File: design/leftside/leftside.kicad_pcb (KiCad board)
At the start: 4 copper layers, 142.6 x 96.2 mm, 211 parts, among them IC2 XC9148G50CER-G, IC3 nRF52833-QDAA-R7, IC4 74AHCT125PW,118, IC5 MCP23018T-E_SS, IC6 XC9291B33D1R-G, J1 USB_C_Receptacle_USB2.0_16P, J2 Battery Pos, J3 Battery Neg, J4 OLED_128x32, J6 Conn_01x04, J7 F32Q-1A7H1-11012, U1 BQ27441-G1, U2 BQ24072RGT, U3 USB6B1, U5 PEC11L-4015F-S0015, U6 PEC11L-4015F-S0015, Y1 ECS-320-8-37B2-JTY-TR

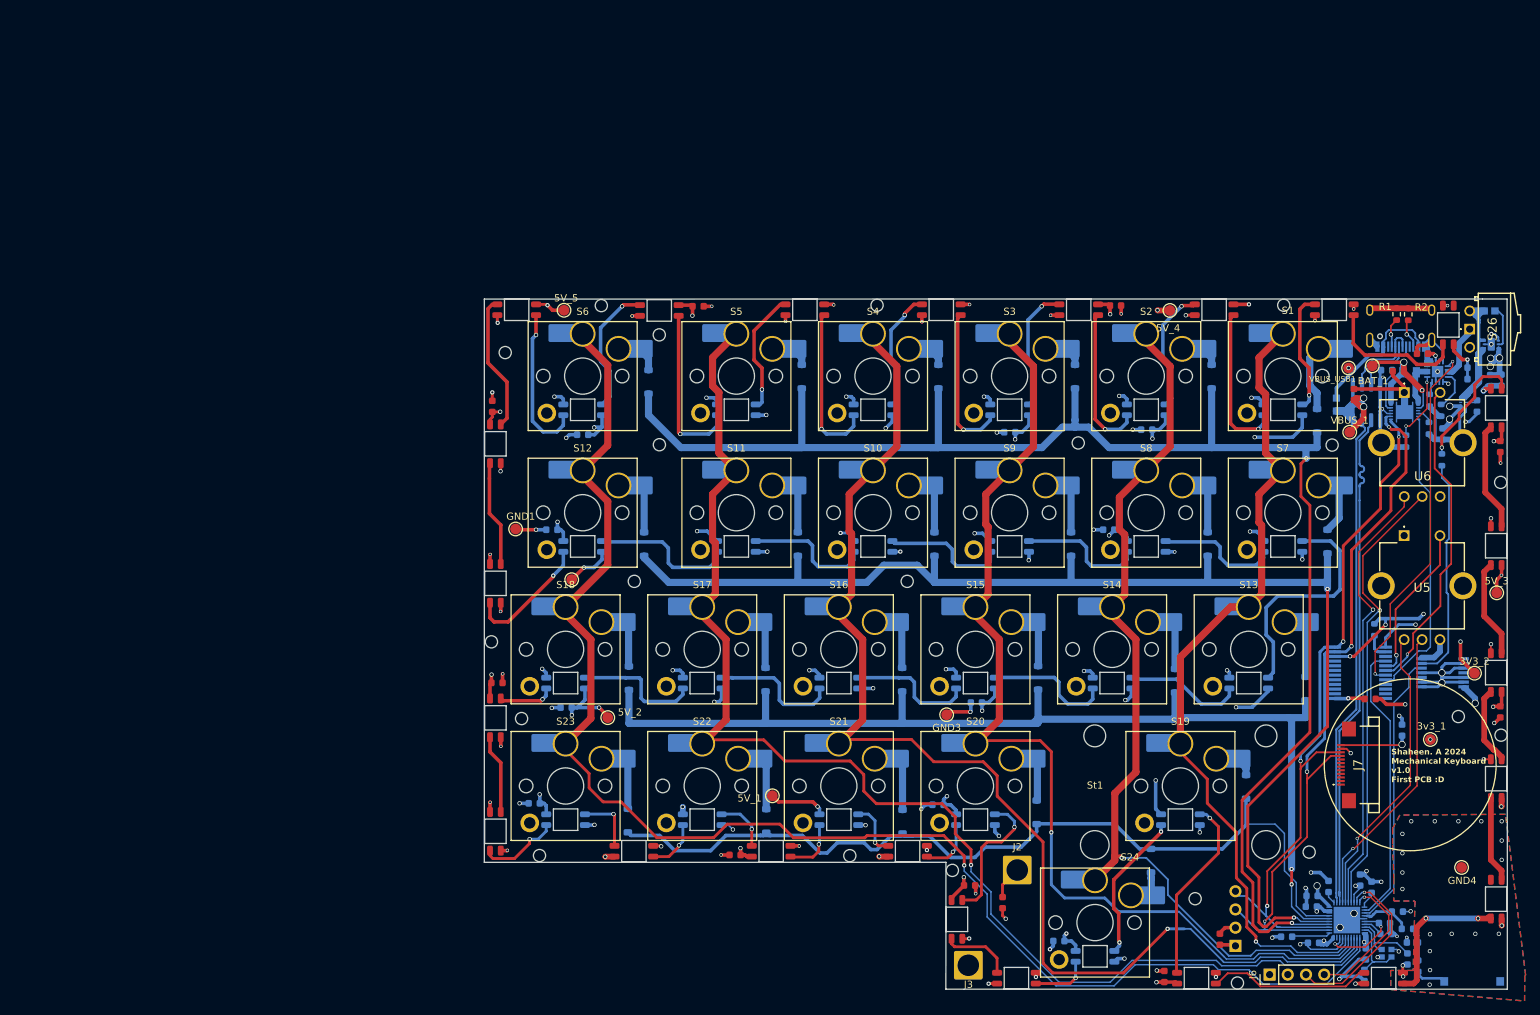
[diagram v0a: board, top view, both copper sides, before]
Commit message: expand power planes
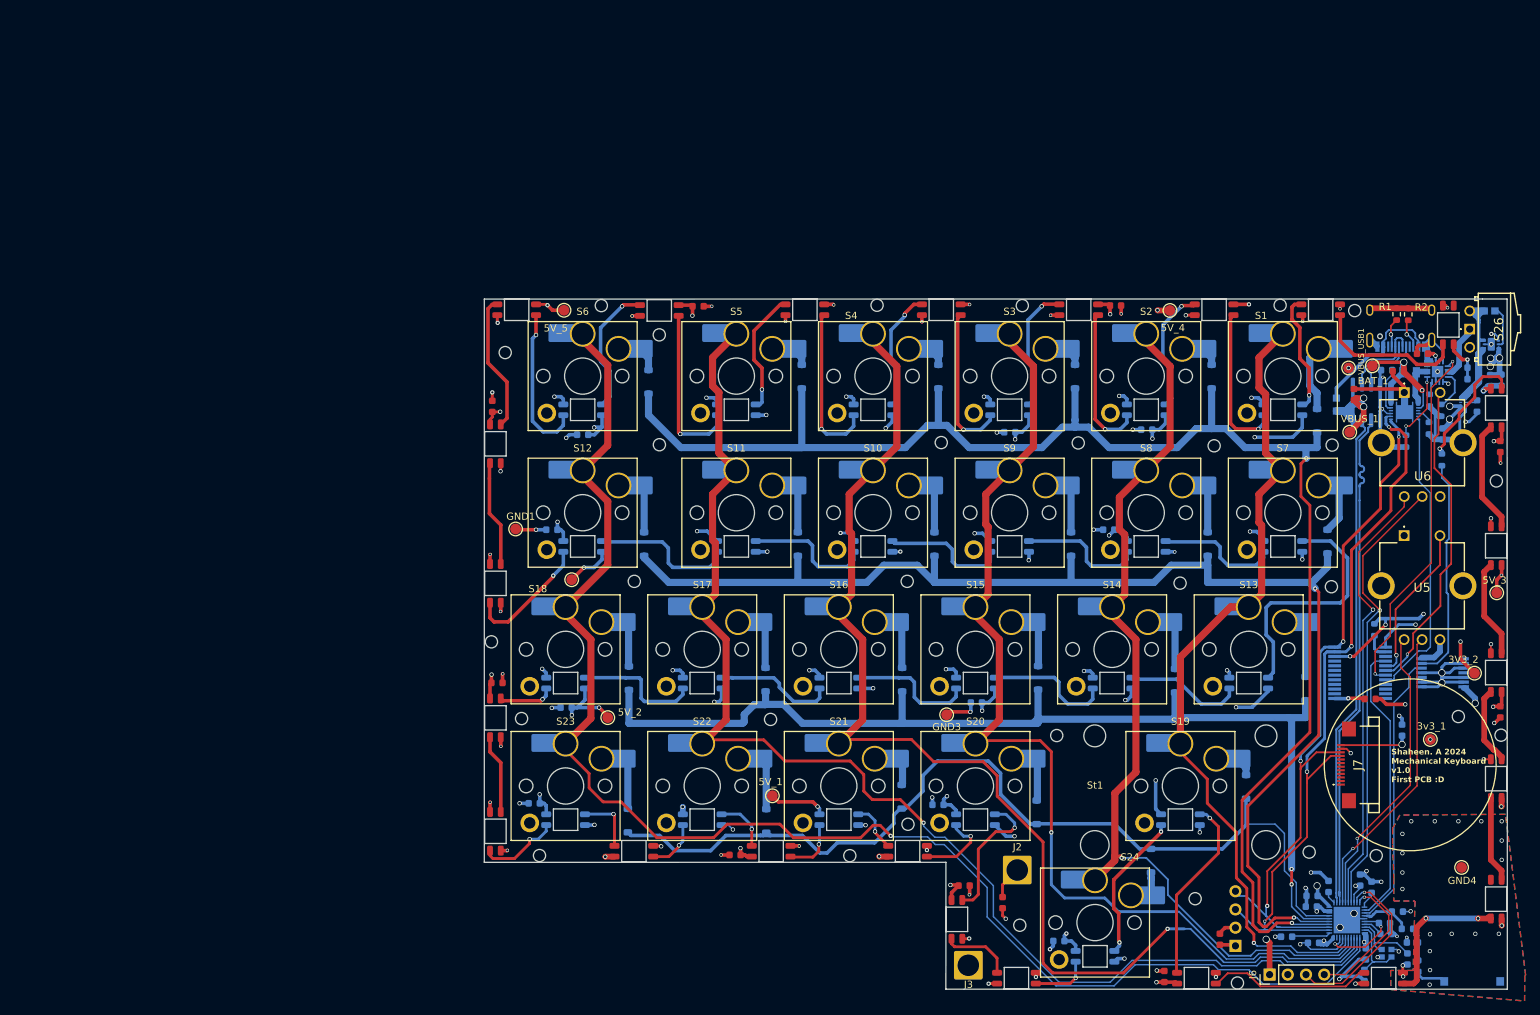
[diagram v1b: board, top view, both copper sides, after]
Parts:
- added REF**: M1.6 Hole, CustomLibrary:M1.6 Hole, F.Cu at (147.2, 75.0)
- added REF**: M1.6 Hole, CustomLibrary:M1.6 Hole, F.Cu at (158.2, 142.3)
- added REF**: M1.6 Hole, CustomLibrary:M1.6 Hole, F.Cu at (163.3, 115.9)
- added REF**: M1.6 Hole, CustomLibrary:M1.6 Hole, F.Cu at (180.5, 94.6)
- added REF**: M1.6 Hole, CustomLibrary:M1.6 Hole, F.Cu at (185.3, 75.5)
- added REF**: M1.6 Hole, CustomLibrary:M1.6 Hole, F.Cu at (207.9, 132.6)
- added REF**: M1.6 Hole, CustomLibrary:M1.6 Hole, F.Cu at (123.4, 113.6)
- added REF**: M1.6 Hole, CustomLibrary:M1.6 Hole, F.Cu at (204.9, 56.6)
- added REF**: M1.6 Hole, CustomLibrary:M1.6 Hole, F.Cu at (158.5, 55.9)
- added REF**: M1.6 Hole, CustomLibrary:M1.6 Hole, F.Cu at (201.6, 95.1)
- moved REF** 8.93 mm to (142.6, 128.3)
- moved Di6 3.47 mm to (141.7, 124.4)
- moved D47 1.90 mm to (200.1, 56.5)
- moved C31 0.76 mm to (150.4, 136.8)
- moved REF** 0.63 mm to (224.6, 80.4)
- moved REF** 0.50 mm to (194.5, 55.9)
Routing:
- net 3V3: track 63.9 -> 69.1 mm, vias 14 -> 15
- net /Row 3: track 127.7 -> 132.1 mm
- net Net-(Di6-A): track 7.55 -> 4.13 mm
- net Net-(D12-DOUT): track 8.02 -> 10.8 mm
- net /Column 4: track 181.5 -> 179.3 mm
- net /Row 0: track 218.9 -> 216.8 mm
- net Net-(D26-DOUT): track 33.1 -> 35.1 mm
- net Net-(D47-DOUT): track 19.9 -> 21.5 mm
- net /Row 1: track 181.8 -> 183.3 mm
- net Net-(D22-DOUT): track 18.3 -> 16.9 mm
- net Net-(D13-DOUT): track 7.82 -> 7.01 mm
- net GND: track 270.3 -> 271.0 mm

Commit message: RS LS Complete
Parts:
- moved R6 0.68 mm to (212.5, 65.9)
- moved C23 0.63 mm to (214.3, 63.3)
- moved BAT_1 0.58 mm to (207.5, 64.9)
- moved C18 0.50 mm to (211.1, 65.6)
- moved D10 0.33 mm to (157.4, 149.7)
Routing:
- net Net-(D47-DOUT): track 21.5 -> 22.9 mm
- net GND: track 271.0 -> 271.7 mm
- net 5V: track 168.0 -> 167.4 mm

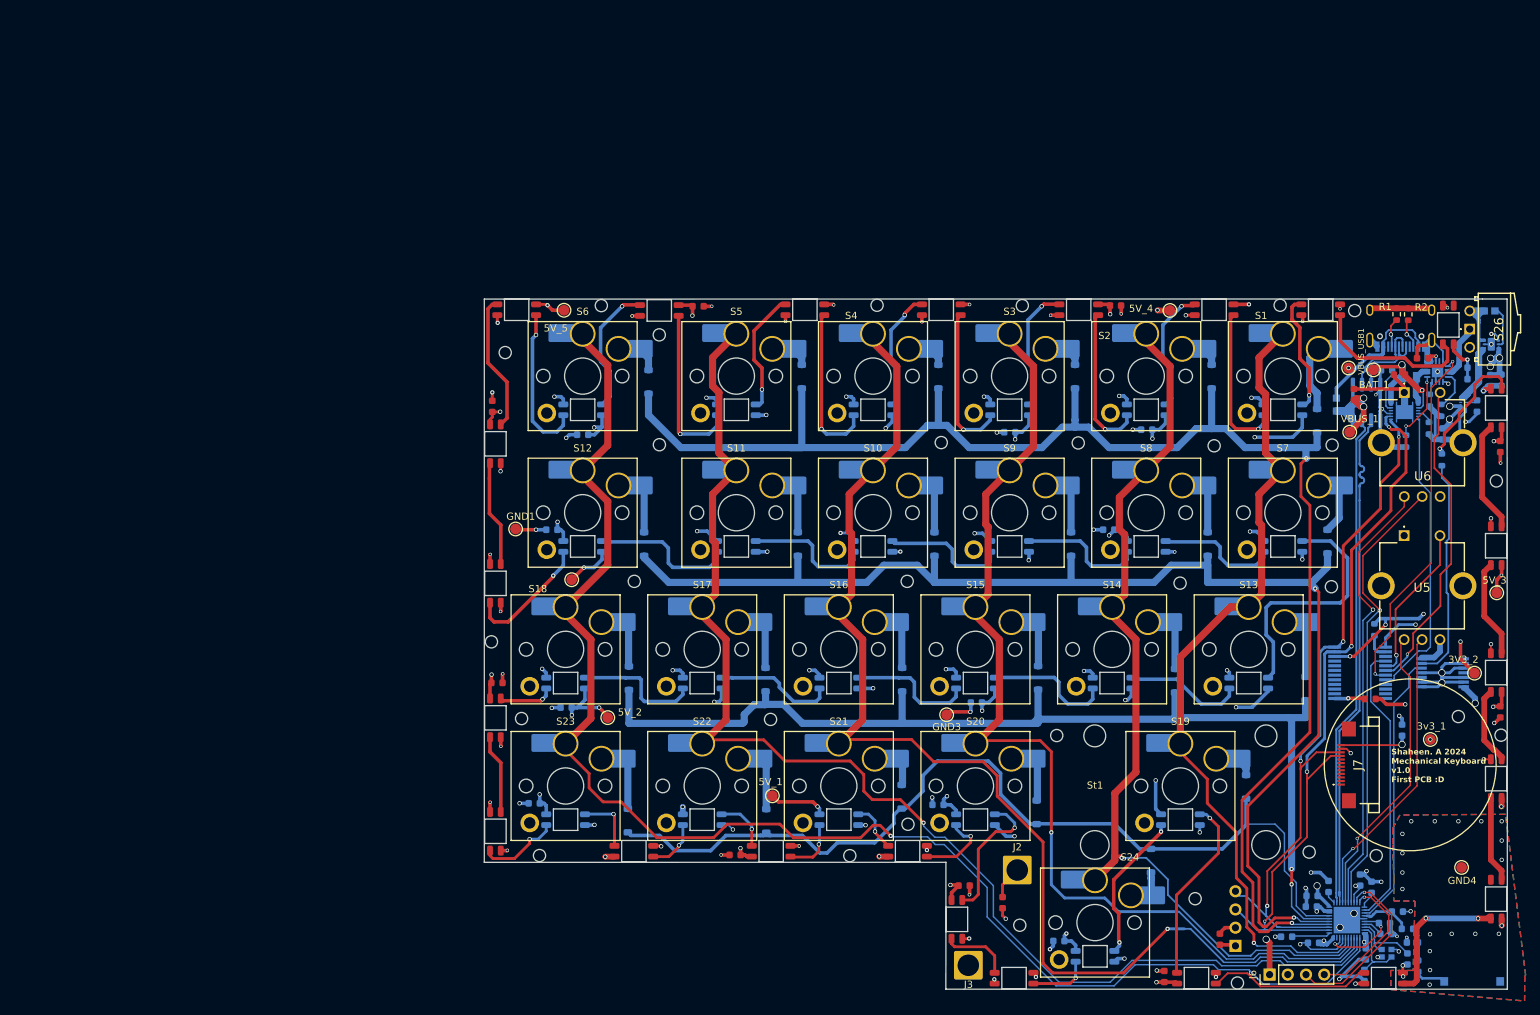
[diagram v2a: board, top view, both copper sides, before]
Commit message: create first merged gerber, prepare to fix board outline
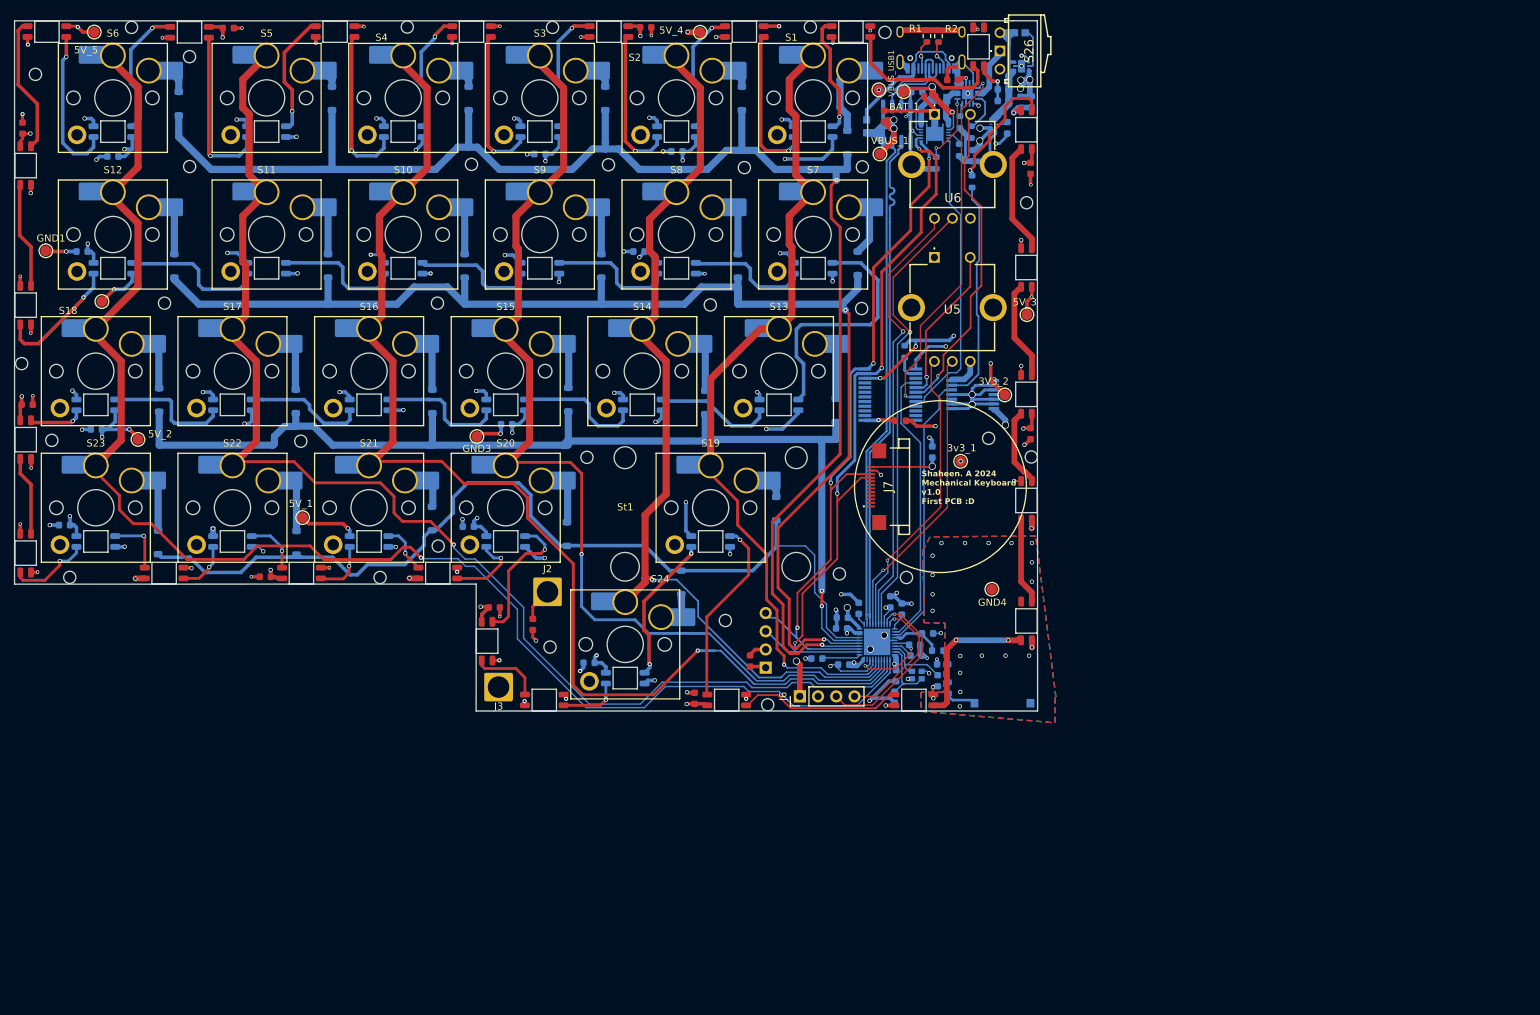
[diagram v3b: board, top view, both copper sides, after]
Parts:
- moved REF** 76.1 mm to (117.1, 99.9)
- moved 3V3_2 76.1 mm to (156.1, 68.4)
- moved 3v3_1 76.1 mm to (149.9, 77.7)
- moved 5V_1 76.1 mm to (58.2, 85.5)
- moved 5V_2 76.1 mm to (35.2, 74.6)
- moved 5V_4 76.1 mm to (113.6, 17.8)
- moved 5V_5 76.1 mm to (29.1, 17.8)
- moved ANT1 76.1 mm to (155.7, 111.4)
- moved BAT_1 76.1 mm to (142.0, 26.1)
- moved C1 76.1 mm to (133.3, 101.0)
- moved C10 76.1 mm to (155.9, 25.8)
- moved C13 76.1 mm to (151.6, 35.1)
- moved C14 76.1 mm to (140.7, 110.6)
- moved C15 76.1 mm to (147.4, 106.0)
- moved C16 76.1 mm to (145.3, 101.7)
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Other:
- outline, holes or cut-outs redrawn

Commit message: submit merged design and do proper outline for boards
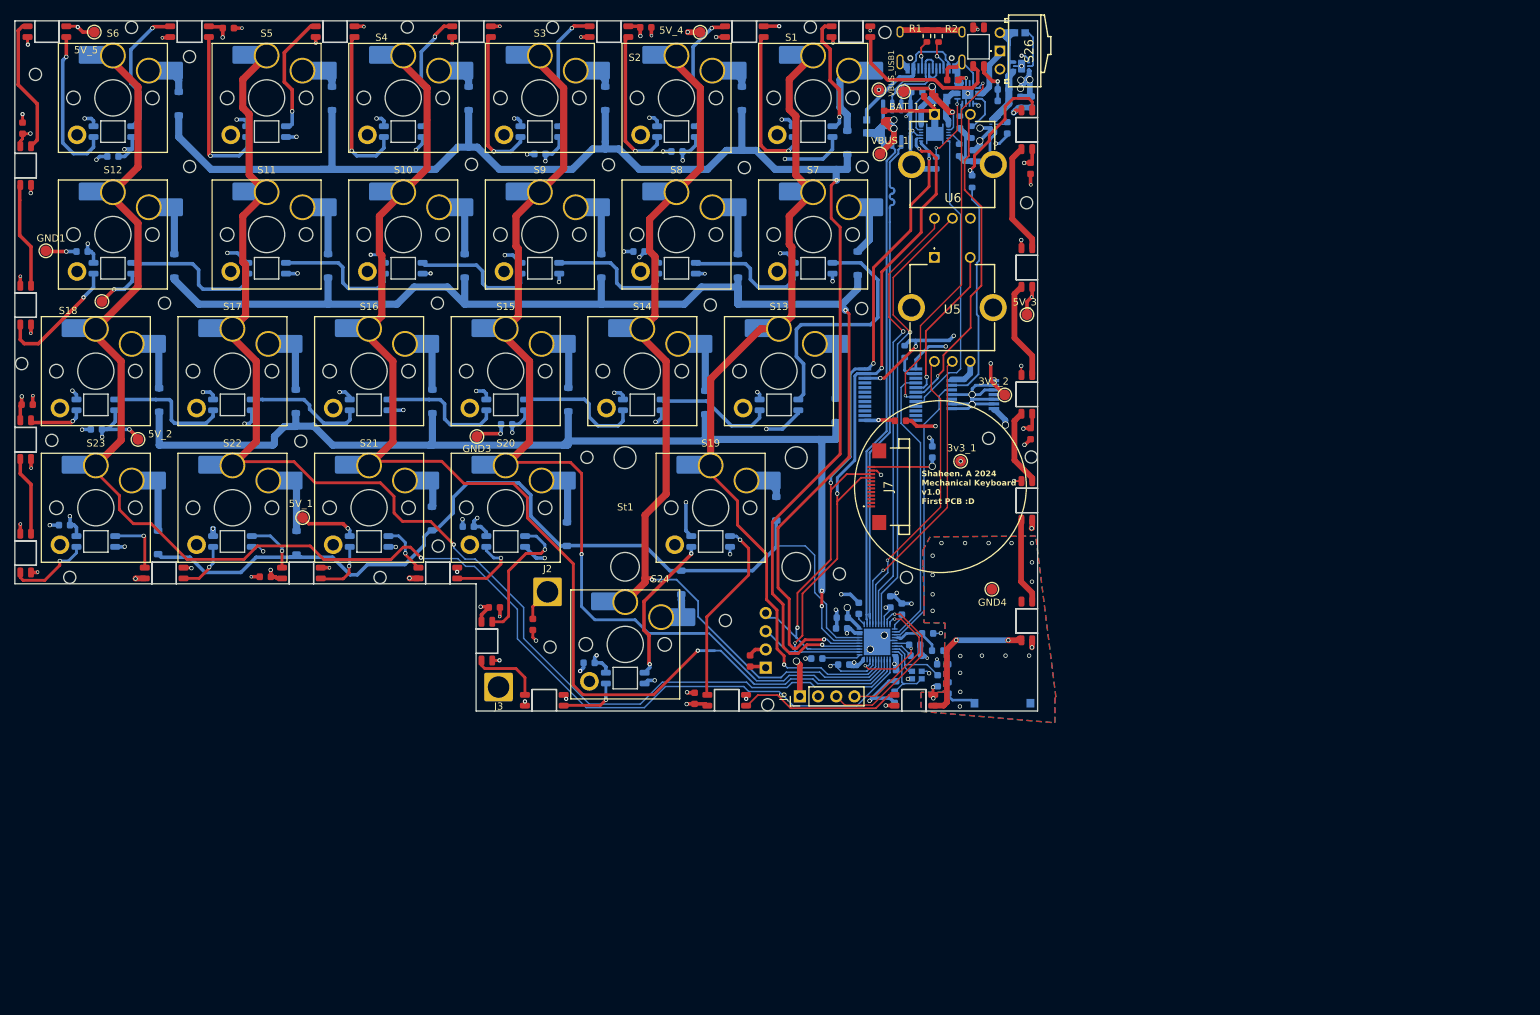
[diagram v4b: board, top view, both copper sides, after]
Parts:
- moved D37 0.09 mm to (42.4, 17.7)
- moved D1 0.05 mm to (159.1, 31.4)
- moved D2 0.05 mm to (159.1, 50.6)
- moved D3 0.05 mm to (159.1, 68.3)
- moved D4 0.05 mm to (159.1, 83.1)
- moved D5 0.05 mm to (159.1, 99.9)
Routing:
- net 5V: track 167.4 -> 166.9 mm
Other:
- outline, holes or cut-outs redrawn
